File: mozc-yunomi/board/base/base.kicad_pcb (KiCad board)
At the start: 2 copper layers, 52.2 x 52.2 mm, 39 parts, among them J1 Conn_01x02_Male, J10 Conn_01x02_Male, J11 Conn_01x02_Male, J12 Conn_01x02_Male, J13 Conn_01x04_Male, J14 Conn_02x03_Odd_Even, J15 Conn_01x01_Male, J16 Conn_01x01_Male, J17 Conn_01x01_Male, J18 Conn_01x01_Male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

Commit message: Rename board directories and add mount hole in base-pcb.
Change-Id: Ia39b7d8c88e6f409046c55b494d820a6e97c7688
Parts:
- added REF**: MountingHole_2.2mm_M2, MountingHole:MountingHole_2.2mm_M2, F.Cu at (159.4, 85.1)
- added REF**: MountingHole_2.2mm_M2, MountingHole:MountingHole_2.2mm_M2, F.Cu at (159.3, 109.2)
- added REF**: MountingHole_2.2mm_M2, MountingHole:MountingHole_2.2mm_M2, F.Cu at (129.7, 109.2)
- added REF**: MountingHole_2.2mm_M2, MountingHole:MountingHole_2.2mm_M2, F.Cu at (129.7, 85.2)

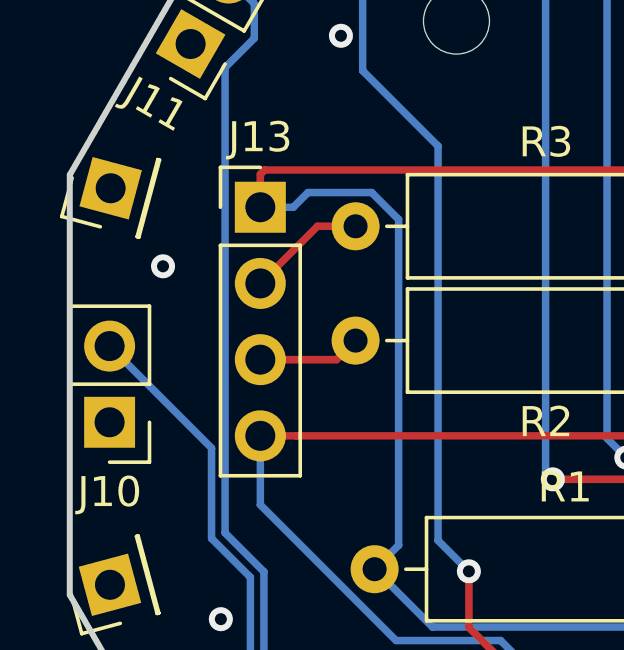
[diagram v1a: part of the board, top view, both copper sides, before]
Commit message: Add silk-screen for USB connector pin assignment.
Change-Id: I3871397b9839605810999388c4ab20431dcb027d
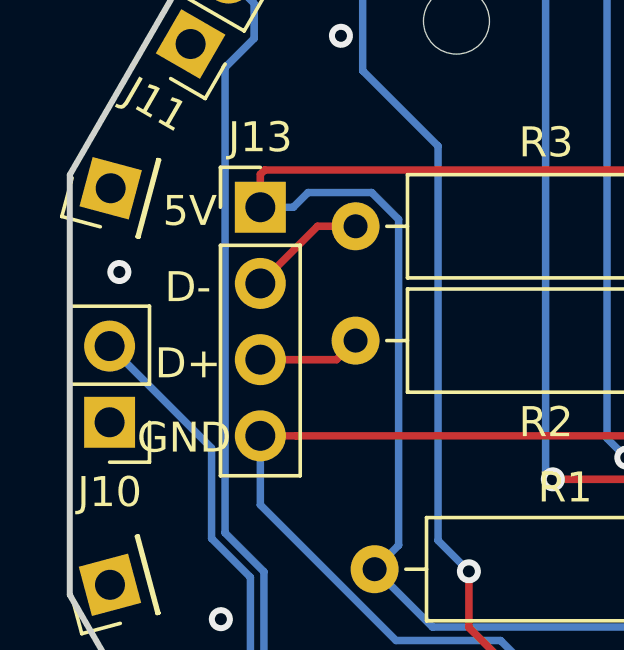
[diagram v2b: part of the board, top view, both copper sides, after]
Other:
- board text added: "5V"
- board text added: "D+"
- board text added: "D-"
- board text added: "GND"
